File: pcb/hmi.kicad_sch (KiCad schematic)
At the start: 4 parts

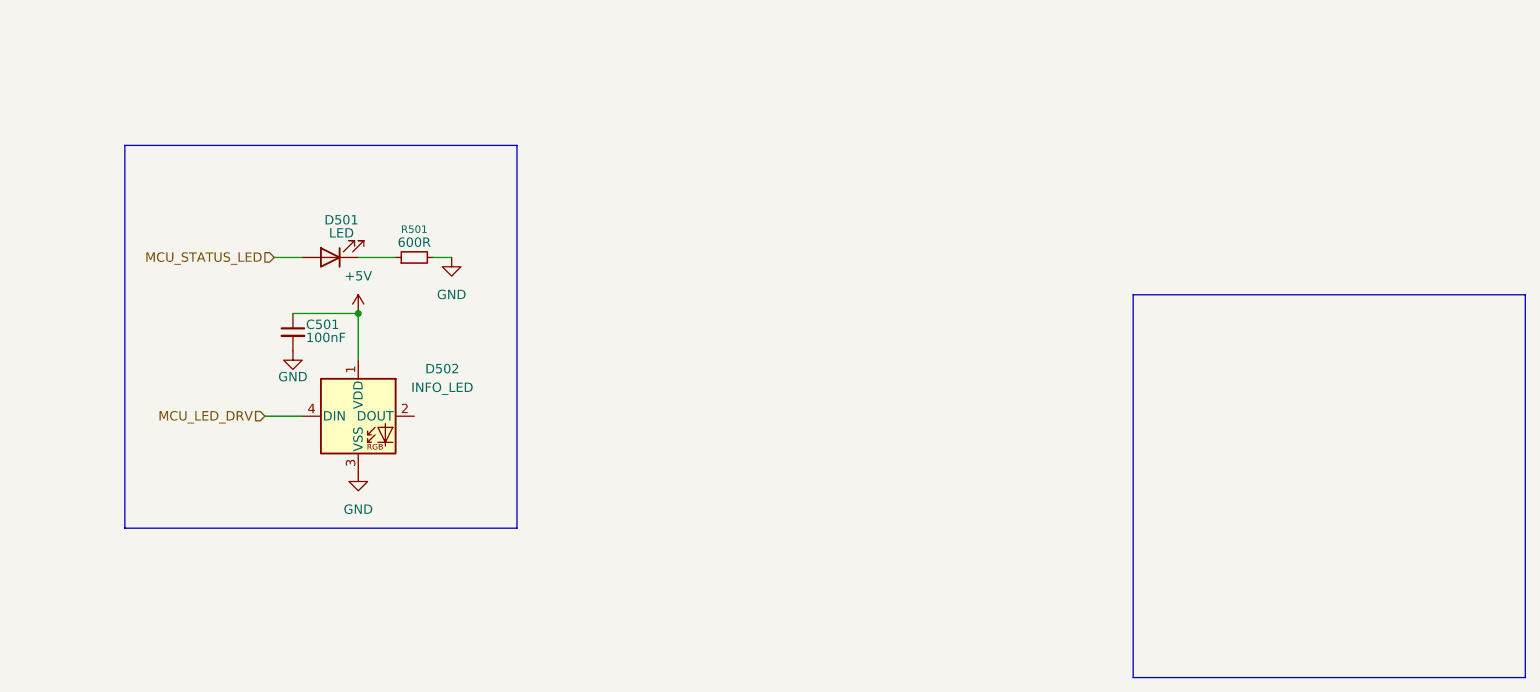
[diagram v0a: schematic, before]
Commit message: dbg uart, nrst, SCS drive, etc
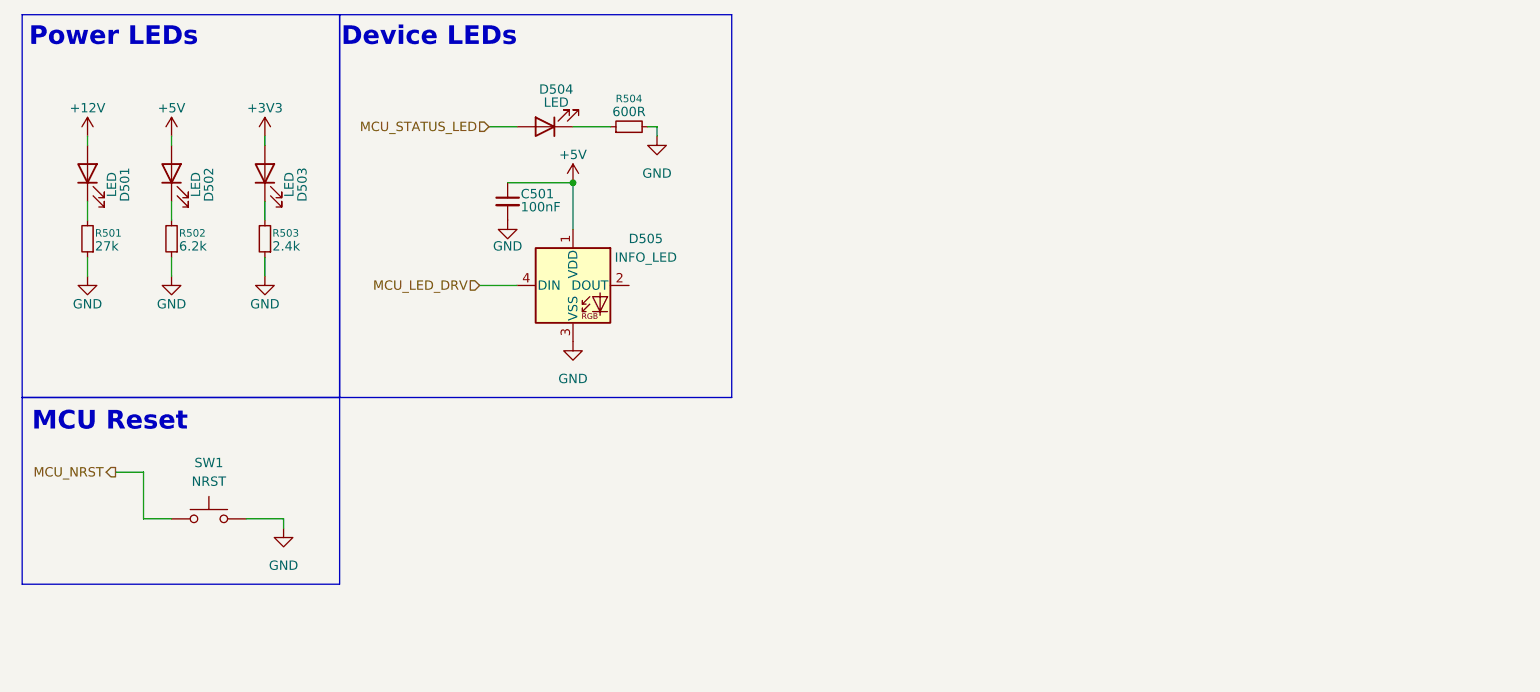
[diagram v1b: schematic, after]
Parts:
- added D501, D502, D503: LED, LED_SMD:LED_0603_1608Metric, symbol Device:LED
- added R501: 27k, Resistor_SMD:R_0402_1005Metric, symbol Device:R_Small
- added R502: 6.2k, Resistor_SMD:R_0402_1005Metric, symbol Device:R_Small
- added R503: 2.4k, Resistor_SMD:R_0402_1005Metric, symbol Device:R_Small
- added SW1: NRST, Button_Switch_SMD:SW_Push_SPST_NO_Alps_SKRK, symbol Switch:SW_Push
- renumbered D501 to D504, D502 to D505, R501 to R504
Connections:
- net +5V: now also D502.2 (A)
- net GND: now also R501.1, R502.1, R503.1, SW1.2
- new net: D502.1 (K), R502.2
- new net: D503.1 (K), R503.2
- new net: D501.1 (K), R501.2
- new net +12V: D501.2 (A)
- new net +3V3: D503.2 (A)
- new net MCU_NRST: SW1.1
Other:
- note added: "Device LEDs"
- note added: "MCU Reset"
- note added: "Power LEDs"
- moved on the sheet: C501, D504, D505, R504

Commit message: connector prep
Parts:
- added TP1: LED_DOUT, symbol Connector:TestPoint
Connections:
- net at D505.2 (DOUT): now also TP1.1
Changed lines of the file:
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@@
+	(wire
+		(pts
+			(xy 104.14 49.53) (xy 104.14 50.8)
+		)
+		(stroke
+			(width 0)
+			(type default)
+		)
+	)
 	(wire
 		(pts
@@
 		(pts
 			(xy 33.02 38.1) (xy 33.02 40.64)
+		)
+		(stroke
+			(width 0)
+			(type default)
+		)
+	)
+	(wire
+		(pts
+			(xy 95.25 49.53) (xy 104.14 49.53)
 		)
 		(stroke
@@
 		)
 	)
+	(symbol
+		(lib_id "Connector:TestPoint")
+		(at 104.14 50.8 180)
+		(unit 1)
+		(exclude_from_sim no)
+		(in_bom yes)
+		(on_board yes)
+		(dnp no)
+		(property "Reference" "TP1"
+			(at 101.6 55.3721 0)
+			(effects
+				(font
+					(size 1.27 1.27)
+				)
+				(justify left)
+			)
+		)
+		(property "Value" "LED_DOUT"
+			(at 103.124 52.832 0)
+			(effects
+				(font
+					(size 1.27 1.27)
+				)
+				(justify left)
+			)
+		)
+		(property "Footprint" ""
+			(at 99.06 50.8 0)
+			(effects
+				(font
+					(size 1.27 1.27)
+				)
+				(hide yes)
+			)
+		)
+		(property "Datasheet" "~"
+			(at 99.06 50.8 0)
+			(effects
+				(font
+					(size 1.27 1.27)
+				)
+				(hide yes)
+			)
+		)
+		(property "Description" "test point"
+			(at 104.14 50.8 0)
+			(effects
+				(font
+					(size 1.27 1.27)
+				)
+				(hide yes)
+			)
+		)
+		(pin "1"
+		)
+		(instances
+			(project ""
+				(path "/0736e313-8db4-41af-b70d-53af7104d2ca/ecaf91e1-a4d1-46c0-9e72-ae26f0cbfbc5"
+					(reference "TP1")
+					(unit 1)
+				)
+			)
+		)
+	)

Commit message: led dout testpoint
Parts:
- TP1: footprint (none) -> TestPoint:TestPoint_Pad_1.0x1.0mm
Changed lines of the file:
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@@
 			)
 		)
-		(property "Footprint" ""
+		(property "Footprint" "TestPoint:TestPoint_Pad_1.0x1.0mm"
 			(at 99.06 50.8 0)
 			(effects
